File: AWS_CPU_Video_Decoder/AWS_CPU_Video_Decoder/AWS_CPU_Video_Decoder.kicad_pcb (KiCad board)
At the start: 2 copper layers, 133.5 x 99.6 mm, 41 parts, among them J1 Conn_02x20_Odd_Even, J10 Conn_01x04_Pin, J11 Conn_01x04_Pin, J12 Conn_01x04_Pin, J13 Conn_01x04_Pin, J14 Conn_01x04_Pin, J15 Conn_01x04_Pin, J2 Conn_01x04_Pin, J3 Video, J4 Conn_01x04_Pin, J5 Conn_02x20_Odd_Even, J6 Conn_01x04_Pin, J7 Conn_01x04_Pin, J8 Conn_01x04_Pin, J9 Conn_01x04_Pin, SW1 Reset

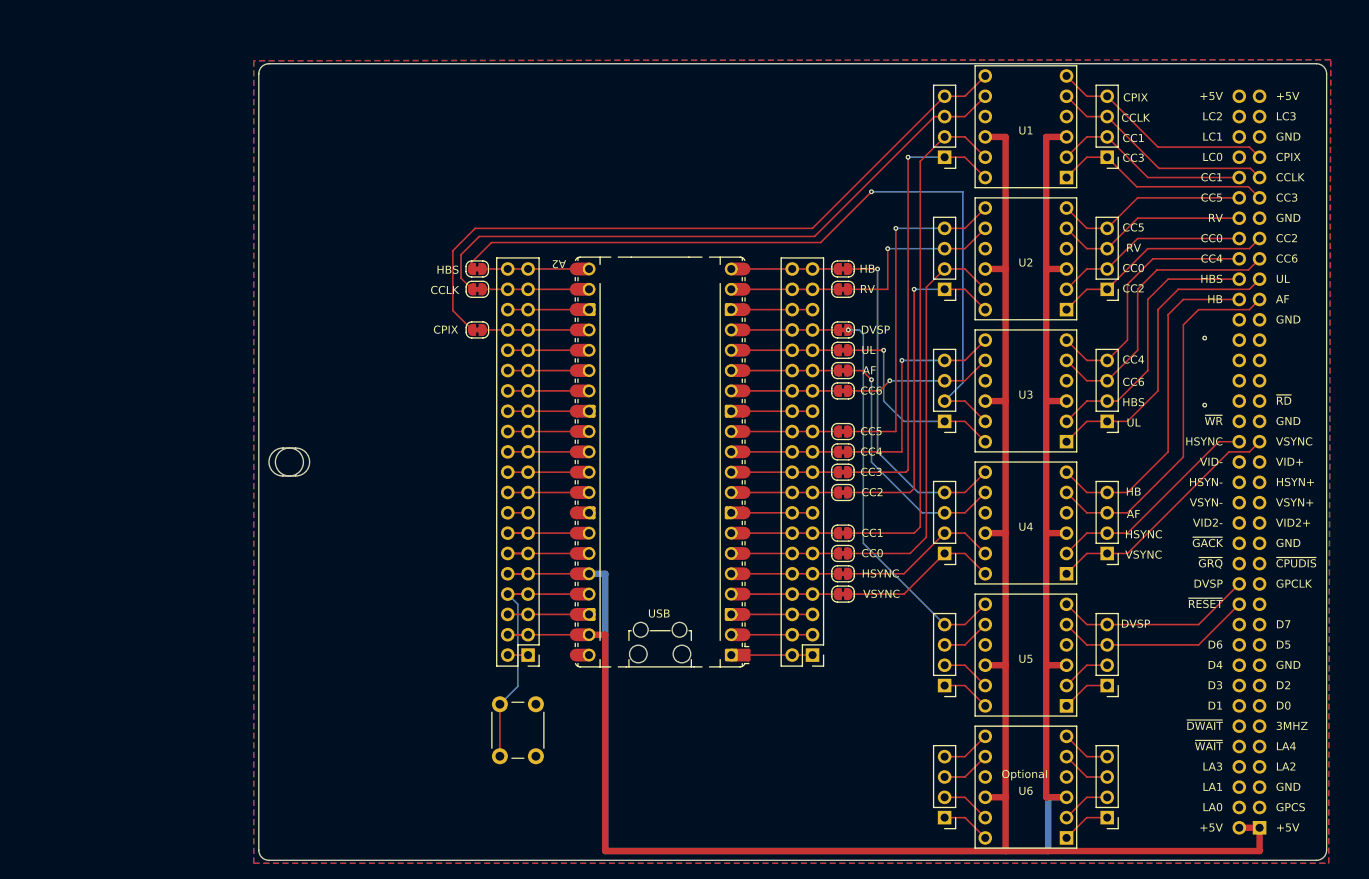
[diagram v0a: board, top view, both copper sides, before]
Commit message: Update PCB to fix floppy drive & update video software to capure all the screen
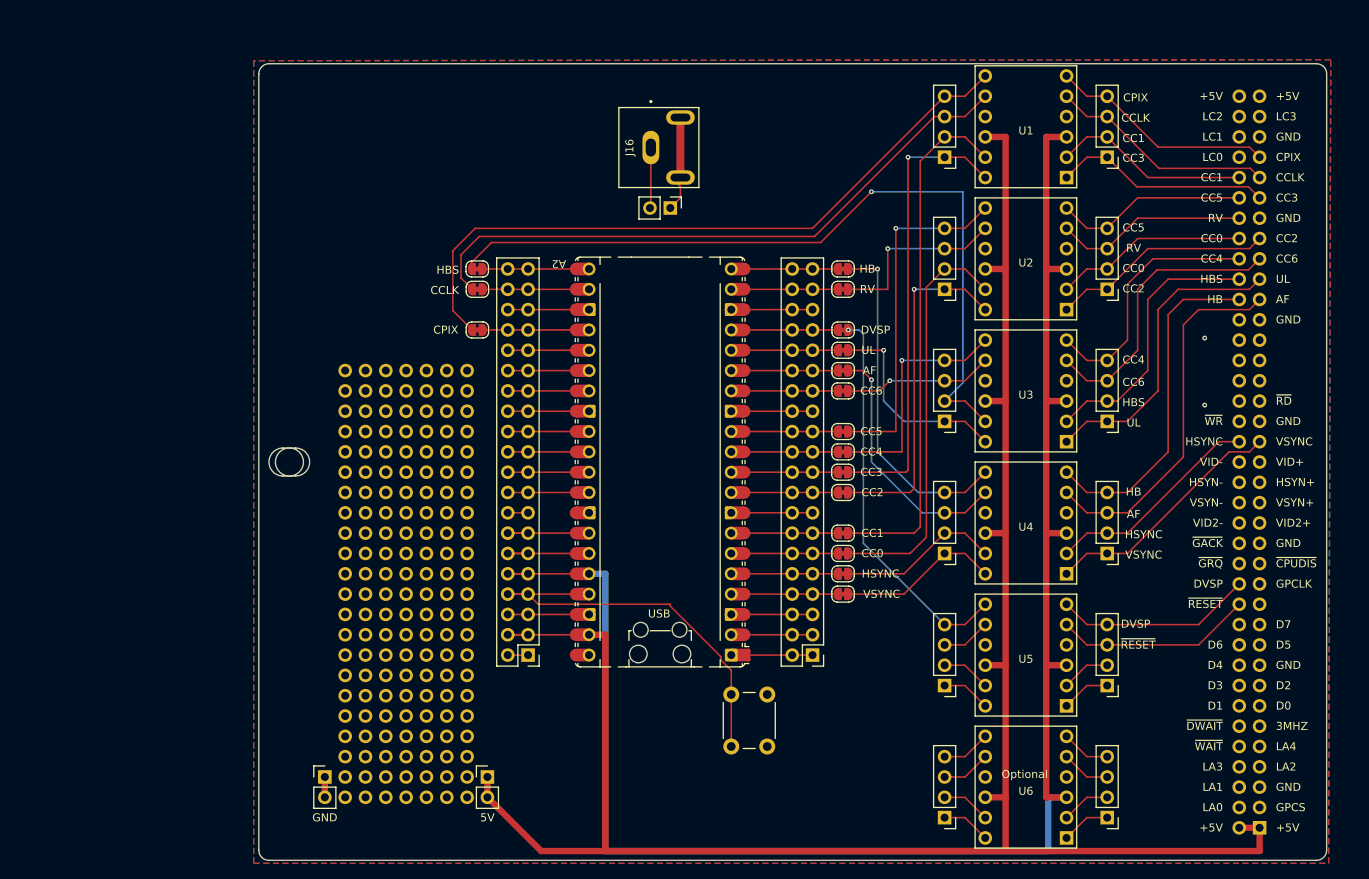
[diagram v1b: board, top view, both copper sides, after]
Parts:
- added ?: , , F.Cu at (124.5, 102.9)
- added ?: , , F.Cu at (134.6, 138.4)
- added ?: , , F.Cu at (121.9, 102.9)
- added ?: , , F.Cu at (134.6, 115.6)
- added ?: , , F.Cu at (124.5, 90.2)
- added ?: , , F.Cu at (134.6, 123.2)
- added ?: , , F.Cu at (134.6, 128.3)
- added ?: , , F.Cu at (121.9, 125.7)
- added ?: , , F.Cu at (124.5, 125.7)
- added ?: , , F.Cu at (129.5, 141.0)
- added ?: , , F.Cu at (132.1, 97.8)
- added ?: , , F.Cu at (121.9, 141.0)
- added ?: , , F.Cu at (129.5, 138.4)
- added ?: , , F.Cu at (129.5, 108.0)
- added ?: , , F.Cu at (119.4, 115.6)
- added ?: , , F.Cu at (132.1, 92.7)
- added ?: , , F.Cu at (127.0, 100.3)
- added ?: , , F.Cu at (127.0, 102.9)
- added ?: , , F.Cu at (119.4, 110.5)
- added ?: , , F.Cu at (127.0, 115.6)
- added ?: , , F.Cu at (119.4, 135.9)
- added ?: , , F.Cu at (127.0, 118.1)
- added ?: , , F.Cu at (134.6, 102.9)
- added ?: , , F.Cu at (127.0, 113.0)
- added ?: , , F.Cu at (129.5, 95.2)
- added ?: , , F.Cu at (129.5, 133.3)
- added ?: , , F.Cu at (132.1, 143.5)
- added ?: , , F.Cu at (127.0, 95.2)
- added ?: , , F.Cu at (134.6, 92.7)
- added ?: , , F.Cu at (127.0, 143.5)
- added ?: , , F.Cu at (134.6, 113.0)
- added ?: , , F.Cu at (129.5, 115.6)
- added ?: , , F.Cu at (119.4, 125.7)
- added ?: , , F.Cu at (132.1, 113.0)
- added ?: , , F.Cu at (124.5, 123.2)
- added ?: , , F.Cu at (119.4, 128.3)
- added ?: , , F.Cu at (132.1, 115.6)
- added ?: , , F.Cu at (119.4, 105.4)
- added ?: , , F.Cu at (132.1, 102.9)
- added ?: , , F.Cu at (129.5, 110.5)
- added ?: , , F.Cu at (124.5, 92.7)
- added ?: , , F.Cu at (121.9, 113.0)
- added ?: , , F.Cu at (124.5, 113.0)
- added ?: , , F.Cu at (124.5, 108.0)
- added ?: , , F.Cu at (119.4, 118.1)
- added ?: , , F.Cu at (127.0, 141.0)
- added ?: , , F.Cu at (119.4, 102.9)
- added ?: , , F.Cu at (119.4, 130.8)
- added ?: , , F.Cu at (134.6, 97.8)
- added ?: , , F.Cu at (121.9, 105.4)
- added ?: , , F.Cu at (132.1, 105.4)
- added ?: , , F.Cu at (121.9, 138.4)
- added ?: , , F.Cu at (124.5, 135.9)
- added ?: , , F.Cu at (127.0, 123.2)
- added ?: , , F.Cu at (121.9, 92.7)
- added ?: , , F.Cu at (127.0, 120.7)
- added ?: , , F.Cu at (134.6, 108.0)
- added ?: , , F.Cu at (134.6, 125.7)
- added ?: , , F.Cu at (132.1, 95.2)
- added ?: , , F.Cu at (119.4, 133.3)
- added ?: , , F.Cu at (127.0, 135.9)
- added ?: , , F.Cu at (124.5, 115.6)
- added ?: , , F.Cu at (121.9, 118.1)
- added ?: , , F.Cu at (124.5, 118.1)
- added ?: , , F.Cu at (119.4, 123.2)
- added ?: , , F.Cu at (121.9, 135.9)
- added ?: , , F.Cu at (134.6, 133.3)
- added ?: , , F.Cu at (127.0, 92.7)
- added ?: , , F.Cu at (129.5, 123.2)
- added ?: , , F.Cu at (124.5, 97.8)
- added ?: , , F.Cu at (124.5, 100.3)
- added ?: , , F.Cu at (127.0, 97.8)
- added ?: , , F.Cu at (124.5, 95.2)
- added ?: , , F.Cu at (119.4, 108.0)
- added ?: , , F.Cu at (132.1, 128.3)
- added ?: , , F.Cu at (132.1, 90.2)
- added ?: , , F.Cu at (127.0, 138.4)
- added ?: , , F.Cu at (129.5, 130.8)
- added ?: , , F.Cu at (119.4, 141.0)
- added ?: , , F.Cu at (129.5, 90.2)
- added ?: , , F.Cu at (134.6, 95.2)
- added ?: , , F.Cu at (121.9, 115.6)
- added ?: , , F.Cu at (129.5, 113.0)
- added ?: , , F.Cu at (124.5, 143.5)
- added ?: , , F.Cu at (134.6, 135.9)
- added ?: , , F.Cu at (132.1, 120.7)
- added ?: , , F.Cu at (119.4, 143.5)
- added ?: , , F.Cu at (119.4, 97.8)
- added ?: , , F.Cu at (124.5, 105.4)
- added ?: , , F.Cu at (127.0, 133.3)
- added ?: , , F.Cu at (119.4, 90.2)
- added ?: , , F.Cu at (132.1, 118.1)
- added ?: , , F.Cu at (132.1, 138.4)
- added ?: , , F.Cu at (129.5, 92.7)
- added ?: , , F.Cu at (132.1, 133.3)
- added ?: , , F.Cu at (129.5, 125.7)
- added ?: , , F.Cu at (129.5, 128.3)
- added ?: , , F.Cu at (129.5, 97.8)
- added ?: , , F.Cu at (127.0, 108.0)
- added ?: , , F.Cu at (124.5, 133.3)
- added ?: , , F.Cu at (129.5, 120.7)
- added ?: , , F.Cu at (132.1, 141.0)
- added ?: , , F.Cu at (121.9, 130.8)
- added ?: , , F.Cu at (132.1, 123.2)
- added ?: , , F.Cu at (124.5, 141.0)
- added ?: , , F.Cu at (129.5, 143.5)
- added ?: , , F.Cu at (124.5, 128.3)
- added ?: , , F.Cu at (134.6, 110.5)
- added ?: , , F.Cu at (119.4, 120.7)
- added ?: , , F.Cu at (127.0, 130.8)
- added ?: , , F.Cu at (127.0, 110.5)
- added ?: , , F.Cu at (134.6, 90.2)
- added ?: , , F.Cu at (129.5, 105.4)
- added ?: , , F.Cu at (121.9, 100.3)
- added ?: , , F.Cu at (121.9, 108.0)
- added ?: , , F.Cu at (129.5, 135.9)
- added ?: , , F.Cu at (121.9, 143.5)
- added ?: , , F.Cu at (134.6, 143.5)
- added ?: , , F.Cu at (127.0, 90.2)
- added ?: , , F.Cu at (134.6, 120.7)
- added ?: , , F.Cu at (129.5, 102.9)
- added ?: , , F.Cu at (119.4, 100.3)
- added ?: , , F.Cu at (132.1, 135.9)
- added ?: , , F.Cu at (134.6, 118.1)
- added ?: , , F.Cu at (132.1, 100.3)
- added ?: , , F.Cu at (121.9, 123.2)
- added ?: , , F.Cu at (132.1, 108.0)
- added ?: , , F.Cu at (119.4, 92.7)
- added ?: , , F.Cu at (119.4, 95.2)
- added ?: , , F.Cu at (124.5, 120.7)
- added ?: , , F.Cu at (121.9, 110.5)
- added ?: , , F.Cu at (121.9, 95.2)
- added ?: , , F.Cu at (124.5, 138.4)
- added ?: , , F.Cu at (134.6, 130.8)
- added ?: , , F.Cu at (119.4, 138.4)
- added ?: , , F.Cu at (124.5, 130.8)
- added ?: , , F.Cu at (134.6, 105.4)
- added ?: , , F.Cu at (119.4, 113.0)
- added ?: , , F.Cu at (121.9, 128.3)
- added ?: , , F.Cu at (127.0, 125.7)
- added ?: , , F.Cu at (121.9, 90.2)
- added ?: , , F.Cu at (134.6, 100.3)
- added ?: , , F.Cu at (132.1, 125.7)
- added ?: , , F.Cu at (129.5, 118.1)
- added ?: , , F.Cu at (132.1, 110.5)
- added ?: , , F.Cu at (127.0, 105.4)
- added ?: , , F.Cu at (121.9, 97.8)
- added ?: , , F.Cu at (132.1, 130.8)
- added ?: , , F.Cu at (127.0, 128.3)
- added ?: , , F.Cu at (121.9, 120.7)
- added ?: , , F.Cu at (121.9, 133.3)
- added ?: , , F.Cu at (134.6, 141.0)
- added ?: , , F.Cu at (129.5, 100.3)
- added ?: , , F.Cu at (124.5, 110.5)
- added J16: Video, local:SWITCHCRAFT_PJRAN1X1U04X, F.Cu at (157.6, 62.3)
- added J17: Conn_01x02_Pin, Connector_PinHeader_2.54mm:PinHeader_1x02_P2.54mm_Vertical, F.Cu at (160.0, 69.8)
- added J18: Conn_01x02_Pin, Connector_PinHeader_2.54mm:PinHeader_1x02_P2.54mm_Vertical, F.Cu at (137.2, 141.0)
- added J19: Conn_01x02_Pin, Connector_PinHeader_2.54mm:PinHeader_1x02_P2.54mm_Vertical, F.Cu at (116.8, 141.0)
- moved SW1 28.9 mm to (167.6, 137.2)
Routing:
- net +5V: track 233.5 -> 253.6 mm
- net P_RESET: track 33.6 -> 51.1 mm
- net Net-(J16-In): track 0.00 -> 11.5 mm
- net Net-(J16-Ext): track 0.00 -> 7.61 mm
- net GND: track 70.5 -> 73.0 mm
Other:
- board text added: "5V"

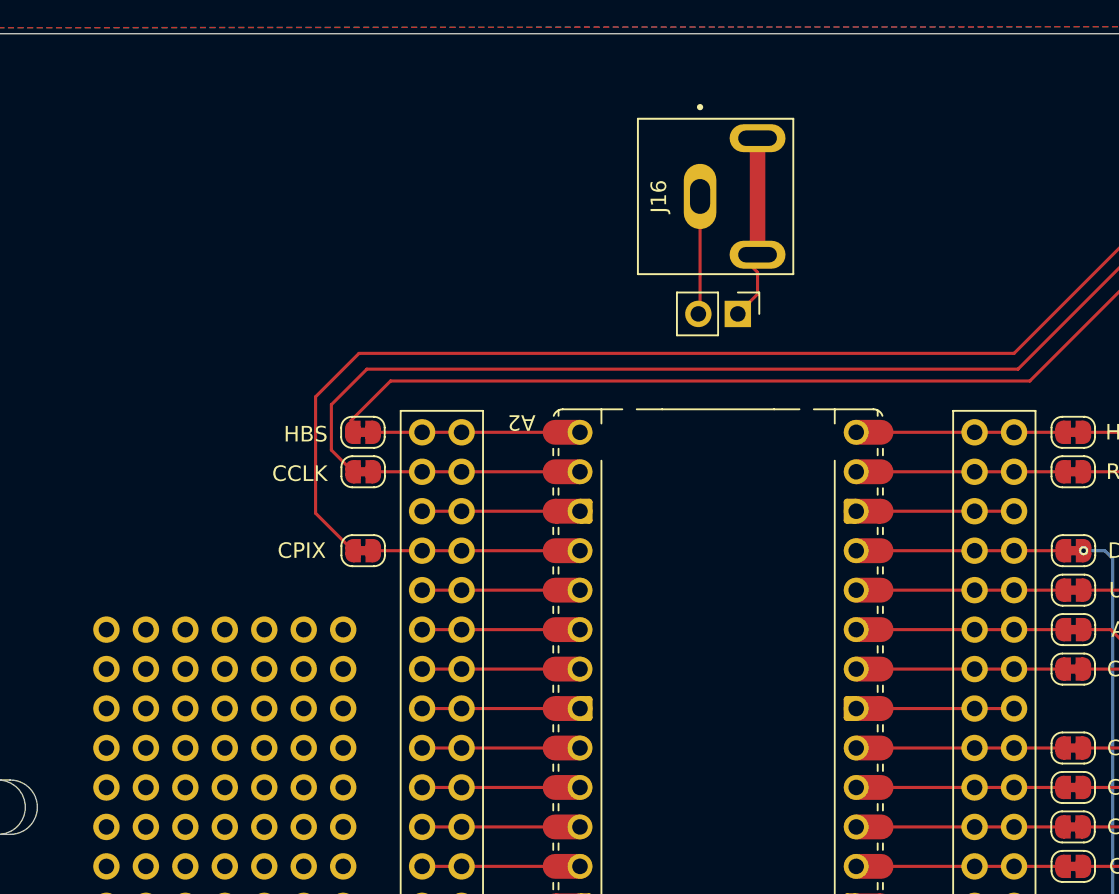
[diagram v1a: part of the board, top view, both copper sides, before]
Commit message: Added basic video
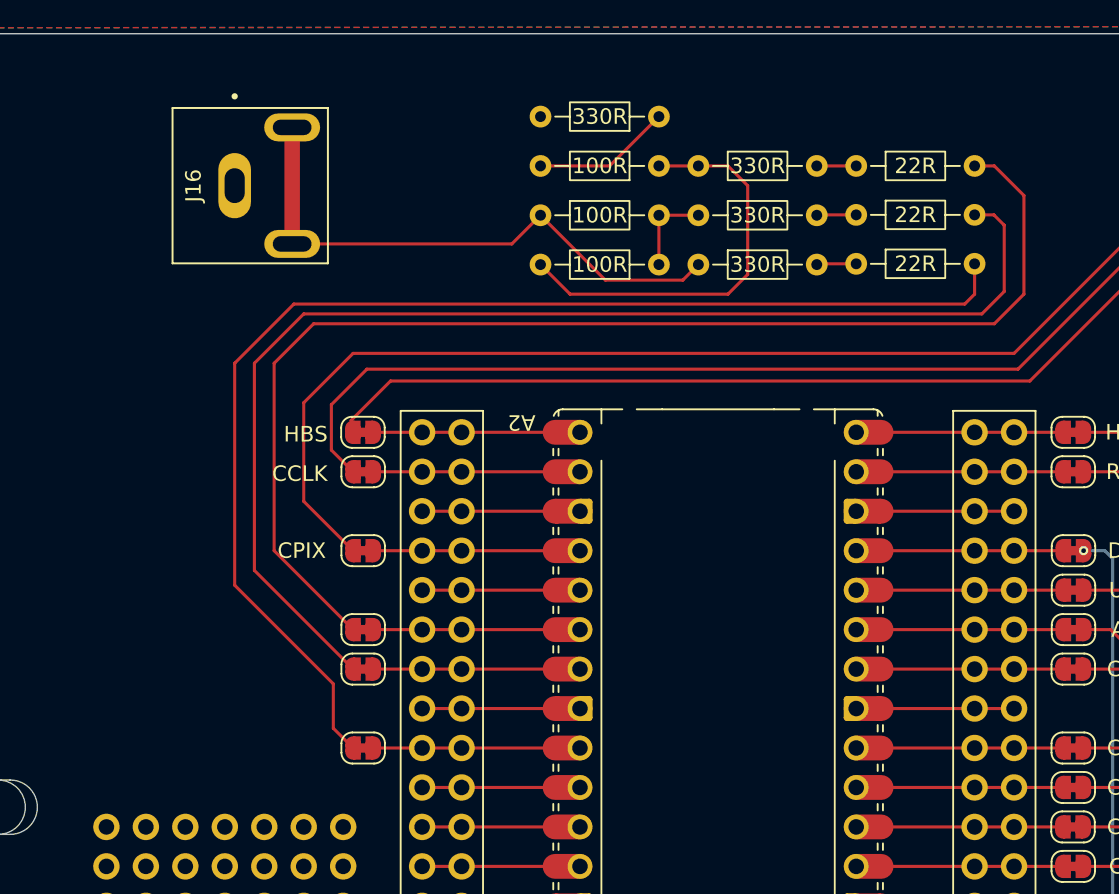
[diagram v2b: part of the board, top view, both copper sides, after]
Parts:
- removed the ? at (124.5, 90.2)
- removed the ? at (132.1, 97.8)
- removed the ? at (132.1, 92.7)
- removed the ? at (127.0, 100.3)
- removed the ? at (129.5, 95.2)
- removed the ? at (127.0, 95.2)
- removed the ? at (134.6, 92.7)
- removed the ? at (124.5, 92.7)
- removed the ? at (134.6, 97.8)
- removed the ? at (121.9, 92.7)
- removed the ? at (132.1, 95.2)
- removed the ? at (127.0, 92.7)
- removed the ? at (124.5, 97.8)
- removed the ? at (124.5, 100.3)
- removed the ? at (127.0, 97.8)
- removed the ? at (124.5, 95.2)
- removed the ? at (132.1, 90.2)
- removed the ? at (129.5, 90.2)
- removed the ? at (134.6, 95.2)
- removed the ? at (119.4, 97.8)
- removed the ? at (119.4, 90.2)
- removed the ? at (129.5, 92.7)
- removed the ? at (129.5, 97.8)
- removed the ? at (134.6, 90.2)
- removed the ? at (121.9, 100.3)
- removed the ? at (127.0, 90.2)
- removed the ? at (119.4, 100.3)
- removed the ? at (132.1, 100.3)
- removed the ? at (119.4, 92.7)
- removed the ? at (119.4, 95.2)
- removed the ? at (121.9, 95.2)
- removed the ? at (121.9, 90.2)
- removed the ? at (134.6, 100.3)
- removed the ? at (121.9, 97.8)
- removed the ? at (129.5, 100.3)
- removed J17: Conn_01x02_Pin, Connector_PinHeader_2.54mm:PinHeader_1x02_P2.54mm_Vertical
- added JP19: Jumper_2_Small_Bridged, Jumper:SolderJumper-2_P1.3mm_Bridged_RoundedPad1.0x1.5mm, F.Cu at (135.9, 97.8)
- added JP20: Jumper_2_Small_Bridged, Jumper:SolderJumper-2_P1.3mm_Bridged_RoundedPad1.0x1.5mm, F.Cu at (135.9, 92.7)
- added JP21: Jumper_2_Small_Bridged, Jumper:SolderJumper-2_P1.3mm_Bridged_RoundedPad1.0x1.5mm, F.Cu at (135.9, 90.2)
- added R1: 22R, Resistor_THT:R_Axial_DIN0204_L3.6mm_D1.6mm_P7.62mm_Horizontal, F.Cu at (167.6, 60.3)
- added R10: 330R, Resistor_THT:R_Axial_DIN0204_L3.6mm_D1.6mm_P7.62mm_Horizontal, F.Cu at (154.9, 57.1)
- added R2: 22R, Resistor_THT:R_Axial_DIN0204_L3.6mm_D1.6mm_P7.62mm_Horizontal, F.Cu at (167.6, 63.5)
- added R3: 22R, Resistor_THT:R_Axial_DIN0204_L3.6mm_D1.6mm_P7.62mm_Horizontal, F.Cu at (167.6, 66.6)
- added R4: 330R, Resistor_THT:R_Axial_DIN0204_L3.6mm_D1.6mm_P7.62mm_Horizontal, F.Cu at (157.5, 60.3)
- added R5: 330R, Resistor_THT:R_Axial_DIN0204_L3.6mm_D1.6mm_P7.62mm_Horizontal, F.Cu at (157.5, 63.5)
- added R6: 330R, Resistor_THT:R_Axial_DIN0204_L3.6mm_D1.6mm_P7.62mm_Horizontal, F.Cu at (157.5, 66.7)
- added R7: 100R, Resistor_THT:R_Axial_DIN0204_L3.6mm_D1.6mm_P7.62mm_Horizontal, F.Cu at (154.9, 60.3)
- added R8: 100R, Resistor_THT:R_Axial_DIN0204_L3.6mm_D1.6mm_P7.62mm_Horizontal, F.Cu at (147.3, 63.5)
- added R9: 100R, Resistor_THT:R_Axial_DIN0204_L3.6mm_D1.6mm_P7.62mm_Horizontal, F.Cu at (154.9, 66.7)
- moved J16 30.0 mm to (127.6, 61.6)
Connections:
- net GPIO20 renamed DAC0
- net GPIO21 renamed DAC1
- net GPIO22 renamed DAC2
- J16 pad 2: Net-(J16-Ext) -> GND
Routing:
- net Net-(JP21-A): track 0.00 -> 79.7 mm
- net Net-(JP19-A): track 0.00 -> 79.3 mm
- net Net-(JP20-A): track 0.00 -> 78.9 mm
- net Net-(R4-Pad1): track 0.00 -> 26.6 mm
- net Net-(J16-In): track 11.5 -> 28.3 mm
- net Net-(R10-Pad1): track 0.00 -> 8.94 mm
- net Net-(J16-Ext): track 7.61 -> 0.00 mm
- net Net-(R5-Pad1): track 0.00 -> 5.71 mm
- net DAC2: track 9.36 -> 12.5 mm
- net DAC1: track 9.36 -> 12.5 mm
- net DAC0: track 9.36 -> 12.5 mm
- net Net-(R3-Pad1): track 0.00 -> 2.56 mm
- net Net-(R2-Pad1): track 0.00 -> 2.55 mm
- net Net-(R1-Pad1): track 0.00 -> 2.54 mm
- net CPIX_LV: track 86.5 -> 87.4 mm

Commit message: Fix level shifters
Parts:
- turned U1 to 0 degrees
- turned U2 to 0 degrees
- turned U3 to 0 degrees
- turned U4 to 0 degrees
- turned U5 to 0 degrees
- turned U6 to 0 degrees
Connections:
- U1 pad 1: CC3 -> CPIX_LV
- U1 pad 11: CC1_LV -> CCLK
- U1 pad 12: CC3_LV -> CPIX
- U1 pad 2: CC1 -> CCLK_LV
- U1 pad 5: CCLK -> CC1_LV
- U1 pad 6: CPIX -> CC3_LV
- U1 pad 7: CPIX_LV -> CC3
- U1 pad 8: CCLK_LV -> CC1
- U2 pad 1: CC2 -> CC5_LV
- U2 pad 11: CC0_LV -> RV
- U2 pad 12: CC2_LV -> CC5
- U2 pad 2: CC0 -> RV_LV
- U2 pad 5: RV -> CC0_LV
- U2 pad 6: CC5 -> CC2_LV
- U2 pad 7: CC5_LV -> CC2
- U2 pad 8: RV_LV -> CC0
- U3 pad 1: UL -> CC4_LV
- U3 pad 11: HBS_LV -> CC6
- U3 pad 12: UL_LV -> CC4
- U3 pad 2: HBS -> CC6_LV
- U3 pad 5: CC6 -> HBS_LV
- U3 pad 6: CC4 -> UL_LV
- U3 pad 7: CC4_LV -> UL
- U3 pad 8: CC6_LV -> HBS
- U4 pad 1: VSYNC -> HB_LV
- U4 pad 11: HSYNC_LV -> AF
- U4 pad 12: VSYNC_LV -> HB
- U4 pad 2: HSYNC -> AF_LV
- U4 pad 5: AF -> HSYNC_LV
- U4 pad 6: HB -> VSYNC_LV
- U4 pad 7: HB_LV -> VSYNC
- U4 pad 8: AF_LV -> HSYNC
- U5 pad 1: unconnected-(J13-Pin_1-Pad1) -> DVSP_LV
- U5 pad 11: unconnected-(J8-Pin_2-Pad2) -> ~{RESET}
- U5 pad 12: unconnected-(J8-Pin_1-Pad1) -> DVSP
- U5 pad 2: unconnected-(J13-Pin_2-Pad2) -> ~{RESET_LV}
- U5 pad 5: ~{RESET} -> unconnected-(J8-Pin_2-Pad2)
- U5 pad 6: DVSP -> unconnected-(J8-Pin_1-Pad1)
- U5 pad 7: DVSP_LV -> unconnected-(J13-Pin_1-Pad1)
- U5 pad 8: ~{RESET_LV} -> unconnected-(J13-Pin_2-Pad2)
- U6 pad 1: unconnected-(J11-Pin_1-Pad1) -> unconnected-(J9-Pin_4-Pad4)
- U6 pad 11: unconnected-(J9-Pin_2-Pad2) -> unconnected-(J11-Pin_3-Pad3)
- U6 pad 12: unconnected-(J9-Pin_1-Pad1) -> unconnected-(J11-Pin_4-Pad4)
- U6 pad 2: unconnected-(J11-Pin_2-Pad2) -> unconnected-(J9-Pin_3-Pad3)
- U6 pad 5: unconnected-(J11-Pin_3-Pad3) -> unconnected-(J9-Pin_2-Pad2)
- U6 pad 6: unconnected-(J11-Pin_4-Pad4) -> unconnected-(J9-Pin_1-Pad1)
- U6 pad 7: unconnected-(J9-Pin_4-Pad4) -> unconnected-(J11-Pin_1-Pad1)
- U6 pad 8: unconnected-(J9-Pin_3-Pad3) -> unconnected-(J11-Pin_2-Pad2)
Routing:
- net HBS_LV: track 99.2 -> 84.0 mm
- net +3V3: track 210.8 -> 204.2 mm
- net +5V: track 253.6 -> 254.9 mm
- net GND: vias 2 -> 14
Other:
- board size 133.5 x 99.6 mm -> 132 x 99.6 mm
